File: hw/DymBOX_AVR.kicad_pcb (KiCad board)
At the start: 2 copper layers, 70.2 x 144.1 mm, 49 parts, among them J4 DS18B20, J5 Conn_02x05_Odd_Even, J6 Conn_01x01_Pin, J7 Conn_01x01_Pin, J8 Conn_01x01_Pin, J9 Conn_01x01_Pin, K1 RT314A24, Q1 BC327, Q2 BC327, Q3 BS170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

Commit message: prace
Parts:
- removed J7, J8, J9: Conn_01x01_Pin, 2pkstartup:TRM2_62409-1_TEC
- removed SW1: RotaryEncoder_Switch, Rotary_Encoder:RotaryEncoder_Alps_EC12E-Switch_Vertical_H20mm_CircularMountingHoles
- added J1: Conn_01x01_Pin, 2pkstartup:faston_6.3, F.Cu at (84.1, 153.2)
- added J1: Conn_01x02_Pin, TerminalBlock_Phoenix:TerminalBlock_Phoenix_PT-1,5-2-3.5-H_1x02_P3.50mm_Horizontal, F.Cu at (114.7, 98.7)
- added J2: Conn_01x01_Pin, 2pkstartup:faston_6.3, F.Cu at (67.3, 153.2)
- added J3: Conn_01x01_Pin, 2pkstartup:faston_6.3, F.Cu at (117.0, 128.3)
- added SW2: RotaryEncoder_Switch, 2pkstartup:RotaryEncoder_Alps_EC12E-Switch_Vertical_H20mm_CircularMountingHoles, B.Cu at (64.0, 76.7)
- J6: footprint 2pkstartup:TRM2_62409-1_TEC -> 2pkstartup:faston_6.3
- U3: footprint Package_TO_SOT_THT:TO-220-3_Horizontal_TabDown -> Package_TO_SOT_THT:TO-220-3_Vertical
- moved F1 71.4 mm to (55.4, 84.7), turned to -90 degrees
- moved R13 62.4 mm to (111.6, 47.5)
- moved J4 61.6 mm to (114.8, 61.1), turned to 90 degrees
- moved J6 36.2 mm to (117.0, 144.6), turned to 90 degrees
- moved D3 24.5 mm to (64.0, 101.7)
- moved C2 21.8 mm to (65.0, 92.3)
- moved C1 20.8 mm to (81.9, 92.7)
- moved C3 14.5 mm to (68.7, 99.1), turned to -90 degrees
- moved R10 14.5 mm to (82.4, 52.7)
- moved Q4 14.2 mm to (102.5, 105.0)
- moved R17 14.2 mm to (105.0, 95.6)
- moved R15 14.2 mm to (102.5, 95.6)
- moved U3 9.66 mm to (74.0, 103.6)
- moved Q1 9.65 mm to (78.2, 46.4)
- moved Q3 9.50 mm to (112.0, 85.0)
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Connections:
- K1 pad 14: Net-(J9-Pin_1) -> Net-(J6-Pin_1)
- TR1 pad 5: Net-(J6-Pin_1) -> Net-(J1-Pin_1)
- U2 pad 12: unconnected-(U2-CA1-Pad12) -> Net-(Q5-C)
- U2 pad 6: Net-(Q1-C) -> unconnected-(U2-CA4-Pad6)
- U2 pad 8: Net-(Q2-C) -> Net-(Q1-C)
- U2 pad 9: Net-(Q5-C) -> Net-(Q2-C)
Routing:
- net +5V: track 203.0 -> 28.1 mm
- net +12V: track 114.8 -> 0.00 mm
- net /SEG_B: track 56.9 -> 0.00 mm
- net /SEG_F: track 51.3 -> 0.00 mm
- net /SEG_A: track 49.4 -> 0.00 mm
- net /MOSI: track 41.1 -> 0.00 mm
- net Net-(U1-PB2): track 39.7 -> 0.00 mm
- net Net-(J4-Pin_2): track 39.5 -> 0.00 mm
- net /RESET: track 37.9 -> 0.00 mm
- net Net-(D3-+): track 34.5 -> 0.00 mm
- net /DT: track 32.9 -> 0.00 mm
- net /DIG_1: track 32.5 -> 0.00 mm
- net /DIG_2: track 29.5 -> 0.00 mm
- net /BTN: track 24.8 -> 0.00 mm
- net /CLK: track 24.0 -> 0.00 mm
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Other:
- board size 70.2 x 144.1 mm -> 70.2 x 135 mm

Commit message: uprava a více
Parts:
- removed the J1 at (114.7, 98.7)
- removed REF** (x4): MountingHole_4.3mm_M4_Pad_TopBottom, MountingHole:MountingHole_4.3mm_M4_Pad_TopBottom
- added J7: Screw_Terminal_01x02, TerminalBlock_Phoenix:TerminalBlock_Phoenix_PT-1,5-2-3.5-H_1x02_P3.50mm_Horizontal, F.Cu at (114.4, 98.0)
- J4: value DS18B20 -> Screw_Terminal_01x03; footprint Connector_Wire:SolderWire-0.127sqmm_1x03_P3.7mm_D0.48mm_OD1mm -> TerminalBlock_Phoenix:TerminalBlock_Phoenix_PT-1,5-3-3.5-H_1x03_P3.50mm_Horizontal
- moved R13 11.7 mm to (108.3, 58.7), turned to 90 degrees
- moved R1 6.43 mm to (77.5, 82.1), turned to 180 degrees
- moved J1 2.67 mm to (86.7, 153.2)
- moved J4 1.52 mm to (115.4, 59.7)
- moved R15 1.24 mm to (101.3, 95.8)
- moved R17 1.24 mm to (103.8, 95.8)
- moved Q5 1.04 mm to (93.6, 46.0)
- moved R10 1.04 mm to (83.4, 52.5)
- moved Q2 1.04 mm to (86.5, 46.0)
- moved R11 1.04 mm to (90.5, 52.4)
- moved R12 1.04 mm to (97.9, 52.4)
- moved Q1 1.03 mm to (79.2, 46.1)
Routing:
- net +12V: track 0.00 -> 100.1 mm
- net +5V: track 28.1 -> 115.9 mm
- net Net-(U1-PB2): track 0.00 -> 26.4 mm
- net Net-(D3-Pad4): track 0.00 -> 22.2 mm
- net Net-(J2-Pin_1): track 0.00 -> 20.0 mm
- net Net-(D2-A): track 0.00 -> 18.8 mm
- net Net-(J1-Pin_1): track 0.00 -> 17.7 mm
- net Net-(D3-+): track 0.00 -> 15.1 mm
- net Net-(D3-Pad3): track 0.00 -> 11.8 mm
- net Net-(D1-A): track 0.00 -> 10.1 mm
- net Net-(U1-PB1): track 0.00 -> 8.14 mm
- net Net-(Q3-G): track 0.00 -> 6.10 mm
- net Net-(Q4-G): track 0.00 -> 5.41 mm

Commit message: úpravy
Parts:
- C1, C2: footprint Capacitor_THT:CP_Radial_D13.0mm_P5.00mm -> Capacitor_THT:CP_Radial_D16.0mm_P7.50mm
- U2: value CA56-12EWA -> FYT-5631BUHR-21; footprint Display_7Segment:CA56-12EWA -> 2pkstartup:FYT-5631BUHR-21
- U3: footprint Package_TO_SOT_THT:TO-220-3_Vertical -> Package_TO_SOT_THT:TO-220-3_Horizontal_TabDown
- moved J4 57.0 mm to (58.4, 58.0), turned to -90 degrees
- moved R13 43.8 mm to (64.5, 59.4), turned to -90 degrees
- moved C2 27.7 mm to (92.4, 96.0)
- moved D3 27.5 mm to (91.4, 102.5)
- moved C5 26.4 mm to (117.4, 77.5), turned to 180 degrees
- moved SW2 25.9 mm to (63.9, 50.8)
- moved U2 20.4 mm to (105.9, 51.5)
- moved Q1 20.4 mm to (99.2, 42.2)
- moved Q2 20.4 mm to (106.5, 42.1)
- moved R11 20.4 mm to (110.5, 48.5)
- moved R12 20.4 mm to (117.9, 48.5)
- moved R2 20.4 mm to (115.4, 36.6)
- moved R8 20.4 mm to (111.9, 38.6)
- moved Q5 20.4 mm to (113.6, 42.1)
- moved R10 20.4 mm to (103.4, 48.6)
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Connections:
- Q1 pad 1: Net-(Q1-C) -> unconnected-(Q1-C-Pad1)
- Q2 pad 1: Net-(Q2-C) -> unconnected-(Q2-C-Pad1)
- Q5 pad 1: Net-(Q5-C) -> unconnected-(Q5-C-Pad1)
- U2 pad 12: Net-(Q5-C) -> unconnected-(U2-CA1-Pad12)
- U2 pad 8: Net-(Q1-C) -> unconnected-(U2-CA3-Pad8)
- U2 pad 9: Net-(Q2-C) -> unconnected-(U2-CA2-Pad9)
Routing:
- net +5V: track 115.9 -> 0.00 mm
- net +12V: track 100.1 -> 10.6 mm
- net Net-(U1-PB2): track 26.4 -> 0.00 mm
- net Net-(D3-Pad4): track 22.2 -> 0.00 mm
- net Net-(D3-+): track 15.1 -> 0.00 mm
- net Net-(D3-Pad3): track 11.8 -> 0.00 mm
- net Net-(D1-A): track 10.1 -> 0.00 mm
- net Net-(U1-PB1): track 8.14 -> 0.00 mm
- net Net-(Q3-G): track 6.10 -> 0.00 mm
- net Net-(U2-b): track 2.43 -> 0.00 mm
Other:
- board size 70.2 x 135 mm -> 70.2 x 133 mm

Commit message: AP63005
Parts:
- removed C2: C_Polarized, Capacitor_THT:CP_Radial_D16.0mm_P7.50mm
- removed C3: C_Small, Capacitor_THT:C_Disc_D5.0mm_W2.5mm_P5.00mm
- removed U3: L7805, Package_TO_SOT_THT:TO-220-3_Horizontal_TabDown
- added C10: 22uF, Capacitor_SMD:C_0805_2012Metric_Pad1.18x1.45mm_HandSolder, F.Cu at (82.9, 94.0)
- added C7: 10uF, Capacitor_SMD:CP_Elec_4x5.8, F.Cu at (78.4, 96.3)
- added C8: 100nF, Capacitor_SMD:C_0805_2012Metric_Pad1.18x1.45mm_HandSolder, F.Cu at (90.9, 95.5)
- added C9: 22uF, Capacitor_SMD:C_0805_2012Metric_Pad1.18x1.45mm_HandSolder, F.Cu at (82.9, 96.0)
- added L1: 4u7H, Inductor_SMD:L_1210_3225Metric_Pad1.42x2.65mm_HandSolder, F.Cu at (87.4, 94.5)
- added U4: AP63205WU, Package_TO_SOT_SMD:TSOT-23-6, F.Cu at (87.3, 98.1)
- C1: value C_Polarized -> 3m3F
- C4, C5: footprint Capacitor_THT:C_Disc_D5.0mm_W2.5mm_P5.00mm -> Capacitor_SMD:C_0805_2012Metric_Pad1.18x1.45mm_HandSolder; moved to B.Cu
- C6: footprint Capacitor_THT:C_Disc_D5.0mm_W2.5mm_P5.00mm -> Capacitor_SMD:C_0805_2012Metric_Pad1.18x1.45mm_HandSolder; moved to F.Cu
- Y1: footprint Crystal:Crystal_HC49-U_Vertical -> Crystal:Crystal_SMD_HC49-SD_HandSoldering; moved to B.Cu
- moved R3 31.3 mm to (93.5, 75.0)
- moved R1 30.6 mm to (60.1, 89.4), turned to 0 degrees
- moved J4 30.3 mm to (88.4, 62.0), turned to 180 degrees
- moved C6 27.5 mm to (83.2, 86.0), turned to 90 degrees
- moved R8 27.0 mm to (106.6, 65.1)
- moved Q5 26.5 mm to (114.7, 68.6)
- moved R10 26.5 mm to (104.3, 75.1)
- moved Q1 26.5 mm to (100.1, 68.6)
- moved Q2 26.5 mm to (107.4, 68.6)
- moved U2 26.5 mm to (106.7, 77.9)
- moved R11 26.5 mm to (111.4, 74.9)
- moved R12 26.5 mm to (118.8, 74.9)
- moved SW2 26.5 mm to (64.8, 77.2)
- moved R2 26.1 mm to (115.5, 62.7)
- moved J5 25.5 mm to (106.9, 87.1)
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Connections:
- C1 pad 1: +5V -> +12V
- Q1 pad 1: unconnected-(Q1-C-Pad1) -> Net-(Q1-C)
- Q2 pad 1: unconnected-(Q2-C-Pad1) -> Net-(Q2-C)
- Q5 pad 1: unconnected-(Q5-C-Pad1) -> Net-(Q5-C)
- U2 pad 12: unconnected-(U2-CA1-Pad12) -> Net-(Q5-C)
- U2 pad 6: unconnected-(U2-CA4-Pad6) -> (no net)
- U2 pad 8: unconnected-(U2-CA3-Pad8) -> Net-(Q1-C)
- U2 pad 9: unconnected-(U2-CA2-Pad9) -> Net-(Q2-C)
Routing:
- net +5V: track 0.00 -> 152.4 mm
- net +12V: track 10.6 -> 99.1 mm
- net /DIG_0: track 0.00 -> 45.5 mm
- net /DIG_1: track 0.00 -> 43.9 mm
- net /DIG_2: track 0.00 -> 40.2 mm
- net Net-(D3-+): track 0.00 -> 35.6 mm
- net /BTN: track 0.00 -> 35.5 mm
- net /DT: track 0.00 -> 34.9 mm
- net Net-(J4-Pin_2): track 0.00 -> 30.7 mm
- net /CLK: track 0.00 -> 30.4 mm
- net Net-(U1-PB7/XTAL2): track 0.00 -> 29.4 mm
- net /MISO: track 0.00 -> 29.1 mm
- net /SCK: track 0.00 -> 29.0 mm
- net /SEG_F: track 0.00 -> 29.0 mm
- net Net-(U2-e): track 0.00 -> 21.5 mm
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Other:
- board size 70.2 x 133 mm -> 70.2 x 106 mm

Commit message: AP63005
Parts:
- removed C7: 10uF, Capacitor_SMD:CP_Elec_4x5.8
- added C2: C_Small, Capacitor_SMD:C_1206_3216Metric_Pad1.33x1.80mm_HandSolder, F.Cu at (78.2, 96.5)
- C6: moved to B.Cu
- TR1: footprint Transformer_THT:Transformer_Breve_TEZ-38x45 -> 2pkstartup:Transformer_Breve_TEZ-38x45
- moved J6 5.00 mm to (116.9, 143.0), turned to -90 degrees
- moved R12 4.81 mm to (117.5, 79.6)
- moved D3 1.34 mm to (82.1, 102.3)
- moved R13 1.07 mm to (86.5, 67.0)
- moved Q1 0.91 mm to (99.2, 68.6)
- moved R10 0.85 mm to (103.5, 74.9)
- moved Q2 0.82 mm to (106.6, 68.6)
- moved J2 0.15 mm to (61.8, 153.1)
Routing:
- net /RESET: track 2.79 -> 71.7 mm
- net /SEG_A: track 14.5 -> 40.0 mm
- net /SEG_F: track 29.0 -> 37.2 mm
- net +12V: track 99.1 -> 94.0 mm
- net /DIG_2: track 40.2 -> 35.4 mm
- net /DIG_0: track 45.5 -> 41.2 mm
- net /DIG_1: track 43.9 -> 47.4 mm
- net Net-(Q5-B): track 2.83 -> 5.25 mm
- net Net-(D3-+): track 35.6 -> 33.9 mm
- net Net-(D3-Pad4): track 9.62 -> 8.31 mm
- net Net-(D3-Pad3): track 19.8 -> 18.4 mm
- net Net-(Q4-G): track 7.46 -> 8.51 mm
- net Net-(J4-Pin_2): track 30.7 -> 31.5 mm
- net Net-(Q2-C): track 12.2 -> 11.4 mm
- net /SEG_G: track 14.9 -> 14.3 mm
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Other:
- board size 70.2 x 106 mm -> 73.2 x 106 mm
- board text added: "500 mA"
- board text added: "DymBOX AVR v1 Rev.1 https://github.com/2pkstartup/DymBOX.git 2pkstartup@gmail.com @2026"
- board text added: "Topná spirála"
- board text added: "~ 230 V"
- board text removed: "DymBOX AVR v1 Rev.1 https://github.com/2pkstartup/dymbox_pcb 2pkstartup@gmail.com @2026"

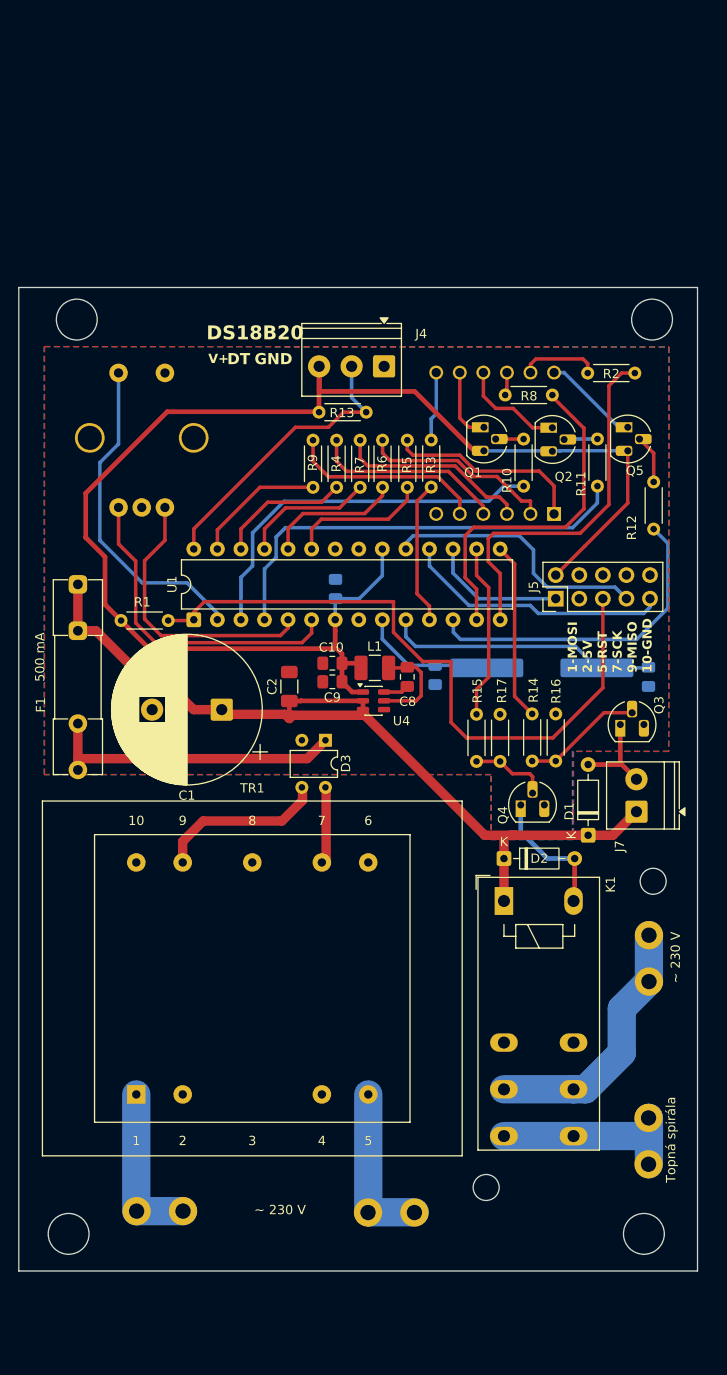
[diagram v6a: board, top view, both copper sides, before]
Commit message: pojistka16A a další
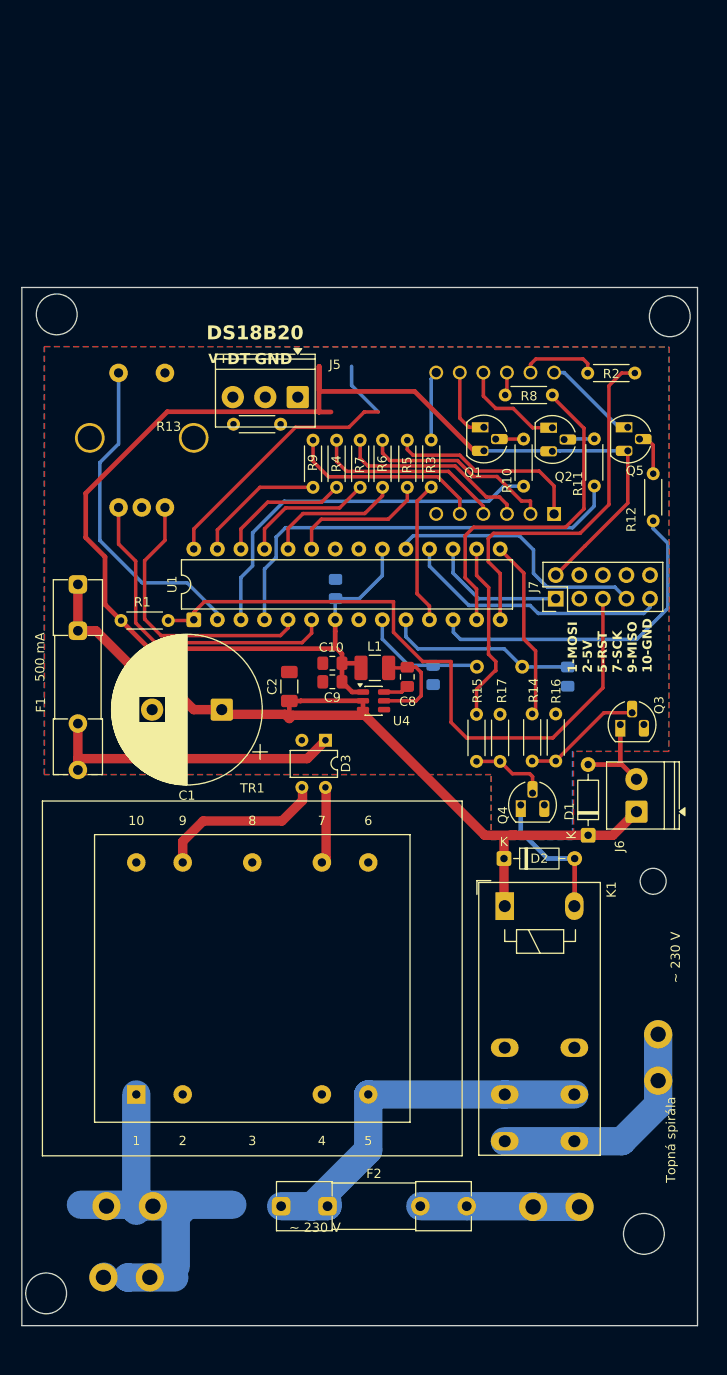
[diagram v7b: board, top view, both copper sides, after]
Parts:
- removed J3: Conn_01x01_Pin, 2pkstartup:faston_6.3
- added F2: 16A, Fuse:Fuseholder_Clip-5x20mm_Littelfuse_111_Inline_P20.00x5.00mm_D1.05mm_Horizontal, F.Cu at (77.3, 152.5)
- added J2: N 230V, 2pkstartup:faston_6.3, F.Cu at (58.2, 160.2)
- C2: value C_Small -> 10uF
- C4: value C_Small -> 22pF
- C5: value Q1 -> 22pF
- D3: value D_Bridge_+-AA -> DB155-YAN
- F1: value Fuse -> 500mA
- J1: value Conn_01x01_Pin -> L 230V
- J2: value Conn_01x01_Pin -> N 230V
- J5: renamed from J4; value Screw_Terminal_01x03 -> TAD05-03-1-L-G
- J6: renamed from J7; value Screw_Terminal_01x02 -> TAD05-02-1-L-G
- J7: renamed from J5; value Conn_02x05_Odd_Even -> ZL202-10G
- Y1: value 16MHz -> 49-8.000MEEJ-B; footprint Crystal:Crystal_SMD_HC49-SD_HandSoldering -> Crystal:Crystal_HC49-U_Vertical
- moved J1 17.8 mm to (104.5, 152.6)
- moved J5 9.88 mm to (79.1, 65.3)
- moved R13 9.31 mm to (77.3, 68.2)
- moved J4 9.07 mm to (118.0, 134.0)
- moved C5 8.72 mm to (108.2, 95.5)
- moved J2 3.29 mm to (58.5, 152.5)
- moved Y1 2.12 mm to (103.3, 94.4)
- moved R12 0.89 mm to (117.4, 78.7)
- moved K1 0.56 mm to (101.4, 120.2)
- moved R11 0.34 mm to (111.1, 74.9)
- moved C4 0.22 mm to (93.7, 95.3)
- renumbered J6 to J4
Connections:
- K1 pad 11: Net-(J3-Pin_1) -> /230V_F16
- TR1 pad 5: Net-(J1-Pin_1) -> Net-(F2-Pad1)
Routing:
- net /230V_F16: track 0.00 -> 36.9 mm
- net Net-(J2-Pin_1): track 17.6 -> 46.2 mm
- net Net-(J3-Pin_1): track 28.2 -> 0.00 mm
- net Net-(U1-PB7/XTAL2): track 29.4 -> 20.6 mm
- net Net-(F2-Pad1): track 0.00 -> 5.44 mm
- net Net-(J4-Pin_1): track 22.3 -> 25.8 mm
- net Net-(J5-Pin_2): track 31.5 -> 33.4 mm
- net +5V: track 151.9 -> 153.2 mm
- net /DIG_2: track 35.4 -> 36.3 mm
- net Net-(U1-PB6/XTAL1): track 14.6 -> 13.7 mm
- net Net-(U1-PB2): track 18.9 -> 19.6 mm
- net Net-(J1-Pin_1): track 17.7 -> 17.2 mm
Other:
- board size 73.2 x 106 mm -> 72.8 x 111.9 mm

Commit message: final v01
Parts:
- removed the J2 at (58.2, 160.2)
- added J3: N 230V, 2pkstartup:faston_6.3, F.Cu at (71.9, 153.5)
- TR1: footprint 2pkstartup:Transformer_Breve_TEZ-38x45 -> Transformer_THT:Transformer_Breve_TEZ-38x45
- moved SW2 6.01 mm to (63.7, 71.3)
- moved C4 6.00 mm to (94.7, 89.4)
- moved C8 6.00 mm to (92.0, 89.6)
- moved D1 6.00 mm to (111.4, 106.6)
- moved J7 6.00 mm to (108.0, 81.1)
- moved R10 6.00 mm to (104.5, 69.0)
- moved R4 6.00 mm to (84.3, 69.1)
- moved R5 6.00 mm to (92.0, 69.1)
- moved R6 6.00 mm to (89.3, 69.1)
- moved R7 6.00 mm to (86.9, 69.1)
- moved R9 6.00 mm to (81.8, 69.1)
- moved J5 6.00 mm to (80.2, 59.4)
- moved R8 6.00 mm to (107.6, 59.2)
- moved C10 6.00 mm to (83.9, 88.1)
- moved C5 6.00 mm to (109.2, 89.5)
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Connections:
- F2 pad 1: Net-(F2-Pad1) -> /230V_F16
- TR1 pad 5: Net-(F2-Pad1) -> /230V_F16
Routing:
- net Net-(J5-Pin_2): track 33.4 -> 20.9 mm
- net Net-(J2-Pin_1): track 46.2 -> 35.3 mm
- net /230V_F16: track 36.9 -> 44.5 mm
- net Net-(F2-Pad1): track 5.44 -> 0.00 mm
- net +5V: track 153.2 -> 156.8 mm
- net Net-(J1-Pin_1): track 17.2 -> 18.9 mm
- net Net-(D3-Pad3): track 18.4 -> 17.4 mm
- net /CLK: track 30.4 -> 29.5 mm
- net /DT: track 34.9 -> 35.8 mm
- net /BTN: track 35.5 -> 36.2 mm
- net Net-(J4-Pin_1): track 25.8 -> 25.1 mm
- net +12V: track 94.4 -> 94.9 mm
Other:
- board size 72.8 x 111.9 mm -> 73 x 112 mm
- board text added: "12V / 500 mA"
- board text added: "12V Fan 12V+ GND"
- board text added: "230 V !!!"
- board text added: "230V L 16 A"
- board text added: "230V N Topna spirala N"
- board text added: "DymBOX AVR v1 Rev.1 https://github.com/2pkstartup/DymBOX 2pkstartup@gmail.com @2026"
- board text added: "Sn:"
- board text added: "Teploměr - DS18B20"
- board text added: "Topná spirála 230V L"
- board text added: "~ 230 V / 16 A"
- board text removed: "500 mA"
- board text removed: "DS18B20"
- board text removed: "DymBOX AVR v1 Rev.1 https://github.com/2pkstartup/DymBOX.git 2pkstartup@gmail.com @2026"
- board text removed: "Topná spirála"
- board text removed: "~ 230 V"
